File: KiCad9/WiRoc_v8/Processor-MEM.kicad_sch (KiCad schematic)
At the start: 28 parts

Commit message: etc
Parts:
- C46, C52: LCSC Part # (none) -> C15525; Manufacturer (none) -> Samsung Electro-Mechanics; ManufacturerPartNumber (none) -> CL05A106MQ5NUNC
- C47, C48, C53, C54, C58, C59: LCSC Part # (none) -> C52923; Manufacturer (none) -> Samsung Electro-Mechanics; ManufacturerPartNumber (none) -> CL05A105KA5NQNC
- U11: value ~ -> AllwinnerH3
- U12: value ~ -> DDR3
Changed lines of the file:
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@@
 			)
 		)
-		(property "Datasheet" "~"
+		(property "Datasheet" "https://jlcpcb.com/api/file/downloadByFileSystemAccessId/8579707174974914560"
 			(at 218.44 43.18 0)
 			(effects
@@
 		)
 		(property "Description" ""
+			(at 218.44 43.18 0)
+			(effects
+				(font
+					(size 1.27 1.27)
+				)
+				(hide yes)
+			)
+		)
+		(property "LCSC Part #" "C52923"
+			(at 218.44 43.18 0)
+			(effects
+				(font
+					(size 1.27 1.27)
+				)
+				(hide yes)
+			)
+		)
+		(property "Manufacturer" "Samsung Electro-Mechanics"
+			(at 218.44 43.18 0)
+			(effects
+				(font
+					(size 1.27 1.27)
+				)
+				(hide yes)
+			)
+		)
+		(property "ManufacturerPartNumber" "CL05A105KA5NQNC"
 			(at 218.44 43.18 0)
 			(effects
@@
 			)
 		)
-		(property "Datasheet" "~"
+		(property "Datasheet" "https://jlcpcb.com/api/file/downloadByFileSystemAccessId/8579707174974914560"
 			(at 207.01 91.44 0)
 			(effects
@@
 		)
 		(property "Description" ""
+			(at 207.01 91.44 0)
+			(effects
+				(font
+					(size 1.27 1.27)
+				)
+				(hide yes)
+			)
+		)
+		(property "LCSC Part #" "C52923"
+			(at 207.01 91.44 0)
+			(effects
+				(font
+					(size 1.27 1.27)
+				)
+				(hide yes)
+			)
+		)
+		(property "Manufacturer" "Samsung Electro-Mechanics"
+			(at 207.01 91.44 0)
+			(effects
+				(font
+					(size 1.27 1.27)
+				)
+				(hide yes)
+			)
+		)
+		(property "ManufacturerPartNumber" "CL05A105KA5NQNC"
 			(at 207.01 91.44 0)
 			(effects
@@
 			)
 		)
-		(property "Datasheet" "~"
+		(property "Datasheet" "https://jlcpcb.com/api/file/downloadByFileSystemAccessId/8579707174974914560"
 			(at 229.87 43.18 0)
 			(effects
@@
 		)
 		(property "Description" ""
+			(at 229.87 43.18 0)
+			(effects
+				(font
+					(size 1.27 1.27)
+				)
+				(hide yes)
+			)
+		)
+		(property "LCSC Part #" "C52923"
+			(at 229.87 43.18 0)
+			(effects
+				(font
+					(size 1.27 1.27)
+				)
+				(hide yes)
+			)
+		)
+		(property "Manufacturer" "Samsung Electro-Mechanics"
+			(at 229.87 43.18 0)
+			(effects
+				(font
+					(size 1.27 1.27)
+				)
+				(hide yes)
+			)
+		)
+		(property "ManufacturerPartNumber" "CL05A105KA5NQNC"
 			(at 229.87 43.18 0)
 			(effects
@@
 			)
 		)
+		(property "LCSC Part #" "C15525"
+			(at 207.01 67.31 0)
+			(effects
+				(font
+					(size 1.27 1.27)
+				)
+				(hide yes)
+			)
+		)
+		(property "Manufacturer" "Samsung Electro-Mechanics"
+			(at 207.01 67.31 0)
+			(effects
+				(font
+					(size 1.27 1.27)
+				)
+				(hide yes)
+			)
+		)
+		(property "ManufacturerPartNumber" "CL05A106MQ5NUNC"
+			(at 207.01 67.31 0)
+			(effects
+				(font
+					(size 1.27 1.27)
+				)
+				(hide yes)
+			)
+		)
 		(pin "2"
 		)
@@
 			)
 		)
-		(property "Datasheet" "~"
+		(property "Datasheet" "https://jlcpcb.com/api/file/downloadByFileSystemAccessId/8579707174974914560"
 			(at 229.87 67.31 0)
 			(effects
@@
 		)
 		(property "Description" ""
+			(at 229.87 67.31 0)
+			(effects
+				(font
+					(size 1.27 1.27)
+				)
+				(hide yes)
+			)
+		)
+		(property "LCSC Part #" "C52923"
+			(at 229.87 67.31 0)
+			(effects
+				(font
+					(size 1.27 1.27)
+				)
+				(hide yes)
+			)
+		)
+		(property "Manufacturer" "Samsung Electro-Mechanics"
+			(at 229.87 67.31 0)
+			(effects
+				(font
+					(size 1.27 1.27)
+				)
+				(hide yes)
+			)
+		)
+		(property "ManufacturerPartNumber" "CL05A105KA5NQNC"
 			(at 229.87 67.31 0)
 			(effects
@@
 			)
 		)
+		(property "LCSC Part #" "C15525"
+			(at 207.01 43.18 0)
+			(effects
+				(font
+					(size 1.27 1.27)
+				)
+				(hide yes)
+			)
+		)
+		(property "Manufacturer" "Samsung Electro-Mechanics"
+			(at 207.01 43.18 0)
+			(effects
+				(font
+					(size 1.27 1.27)
+				)
+				(hide yes)
+			)
+		)
+		(property "ManufacturerPartNumber" "CL05A106MQ5NUNC"
+			(at 207.01 43.18 0)
+			(effects
+				(font
+					(size 1.27 1.27)
+				)
+				(hide yes)
+			)
+		)
 		(pin "2"
 		)
@@
 			)
 		)
-		(property "Datasheet" "~"
+		(property "Datasheet" "https://jlcpcb.com/api/file/downloadByFileSystemAccessId/8579707174974914560"
 			(at 218.44 91.44 0)
 			(effects
@@
 		)
 		(property "Description" ""
+			(at 218.44 91.44 0)
+			(effects
+				(font
+					(size 1.27 1.27)
+				)
+				(hide yes)
+			)
+		)
+		(property "LCSC Part #" "C52923"
+			(at 218.44 91.44 0)
+			(effects
+				(font
+					(size 1.27 1.27)
+				)
+				(hide yes)
+			)
+		)
+		(property "Manufacturer" "Samsung Electro-Mechanics"
+			(at 218.44 91.44 0)
+			(effects
+				(font
+					(size 1.27 1.27)
+				)
+				(hide yes)
+			)
+		)
+		(property "ManufacturerPartNumber" "CL05A105KA5NQNC"
 			(at 218.44 91.44 0)
 			(effects
@@
 			)
 		)
-		(property "Datasheet" "~"
+		(property "Datasheet" "https://jlcpcb.com/api/file/downloadByFileSystemAccessId/8579707174974914560"
 			(at 218.44 67.31 0)
 			(effects
@@
 		)
 		(property "Description" ""
+			(at 218.44 67.31 0)
+			(effects
+				(font
+					(size 1.27 1.27)
+				)
+				(hide yes)
+			)
+		)
+		(property "LCSC Part #" "C52923"
+			(at 218.44 67.31 0)
+			(effects
+				(font
+					(size 1.27 1.27)
+				)
+				(hide yes)
+			)
+		)
+		(property "Manufacturer" "Samsung Electro-Mechanics"
+			(at 218.44 67.31 0)
+			(effects
+				(font
+					(size 1.27 1.27)
+				)
+				(hide yes)
+			)
+		)
+		(property "ManufacturerPartNumber" "CL05A105KA5NQNC"
 			(at 218.44 67.31 0)
 			(effects
@@
 			)
 		)
-		(property "Value" "~"
+		(property "Value" "DDR3"
 			(at 102.87 25.4 0)
 			(effects
@@
 			)
 		)
-		(property "Value" "~"
+		(property "Value" "AllwinnerH3"
 			(at 45.72 64.77 0)
 			(effects

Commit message: add bom
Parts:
- C28, C29, C49, C50, C51, C55, C56, C57, C60, C61, C62, C63: IncludeInBOM (none) -> TRUE; JLCBasicExtended (none) -> Basic; LCSC Part # (none) -> C1525; Manufacturer (none) -> Samsung Electro-Mechanics; ManufacturerPartNumber (none) -> CL05B104KO5NNNC; Package (none) -> 0402
- C46, C47, C48, C52, C53, C54, C58, C59: IncludeInBOM (none) -> TRUE; JLCBasicExtended (none) -> Basic; Package (none) -> 0402
- R18, R20, R21: IncludeInBOM (none) -> TRUE; JLCBasicExtended (none) -> Extended; LCSC Part # (none) -> C25094; Manufacturer (none) -> Uniroyal Elec; ManufacturerPartNumber (none) -> 0402WGF2400TCE; Package (none) -> 0402
- R36, R37: IncludeInBOM (none) -> TRUE; JLCBasicExtended (none) -> Basic; LCSC Part # (none) -> C4109; Manufacturer (none) -> Uniroyal Elec; ManufacturerPartNumber (none) -> 0402WGF2001TCE; Package (none) -> 0402
- R38: IncludeInBOM (none) -> TRUE; JLCBasicExtended (none) -> Basic; LCSC Part # (none) -> C25076; Manufacturer (none) -> Uniroyal Elec; ManufacturerPartNumber (none) -> 0402WGF1000TCE; Package (none) -> 0402
- U11: IncludeInBOM (none) -> TRUE; JLCBasicExtended (none) -> Extended; LCSC Part # (none) -> C94644; Manufacturer (none) -> Allwinner; ManufacturerPartNumber (none) -> H3; Package (none) -> FBGA-347(14x14)
- U12: IncludeInBOM (none) -> TRUE; JLCBasicExtended (none) -> Extended; LCSC Part # (none) -> C2841151; Manufacturer (none) -> Micron Tech; ManufacturerPartNumber (none) -> MT41K128M16JT-107:K; Note (none) -> C2909894 H5TQ2G63GFR-TEC 96ball FBGA compatible pinout : 0 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; Package (none) -> FBGA-96(8x14)

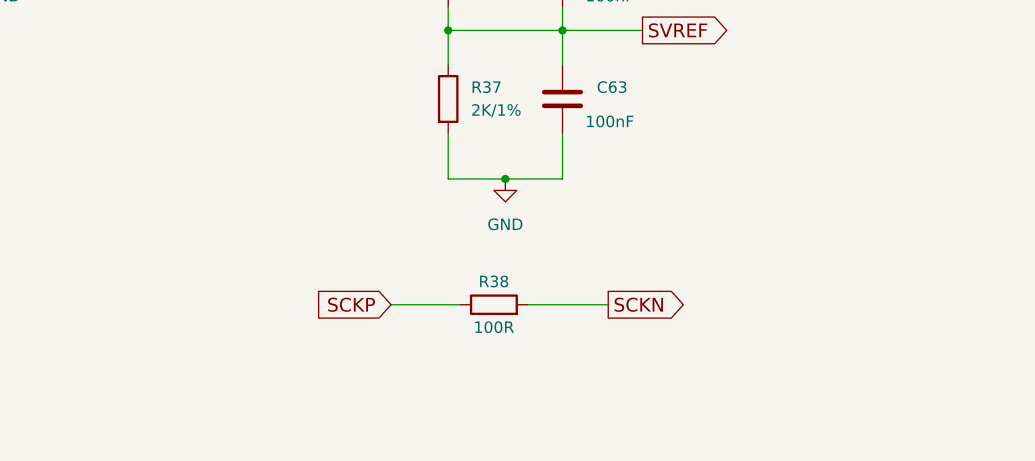
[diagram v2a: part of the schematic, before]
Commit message: change tracewidth for mem, add nettie for better length calculation
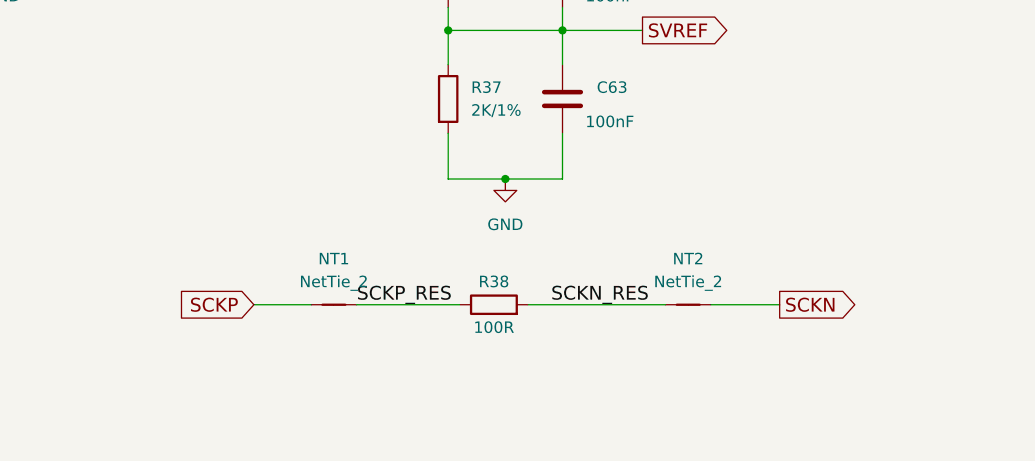
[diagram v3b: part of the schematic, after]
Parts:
- added NT1, NT2: NetTie_2, WiRoc:NetTie-2_SMD_Pad0.12mm, symbol Device:NetTie_2
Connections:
- net SCKN: now also NT2.2; no longer R38.2
- net SCKP: now also NT1.1; no longer R38.1
- new net SCKN_RES: NT2.1, R38.2
- new net SCKP_RES: NT1.2, R38.1
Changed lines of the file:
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@@
 	(wire
 		(pts
-			(xy 198.12 161.29) (xy 205.74 161.29)
+			(xy 182.88 161.29) (xy 189.23 161.29)
 		)
 		(stroke
@@
 	(wire
 		(pts
+			(xy 233.68 161.29) (xy 241.3 161.29)
+		)
+		(stroke
+			(width 0)
+			(type default)
+		)
+	)
+	(wire
+		(pts
 			(xy 229.87 95.25) (xy 241.3 95.25)
 		)
@@
 	(wire
 		(pts
-			(xy 213.36 161.29) (xy 222.25 161.29)
+			(xy 213.36 161.29) (xy 228.6 161.29)
 		)
 		(stroke
@@
 	(wire
 		(pts
+			(xy 194.31 161.29) (xy 205.74 161.29)
+		)
+		(stroke
+			(width 0)
+			(type default)
+		)
+	)
+	(wire
+		(pts
 			(xy 133.35 115.57) (xy 133.35 118.11)
 		)
@@
 		)
 	)
+	(label "SCKN_RES"
+		(at 215.9 161.29 0)
+		(effects
+			(font
+				(size 1.524 1.524)
+			)
+			(justify left bottom)
+		)
+	)
 	(label "SA7"
 		(at 74.93 46.99 0)
@@
 		)
 	)
+	(label "SCKP_RES"
+		(at 194.31 161.29 0)
+		(effects
+			(font
+				(size 1.524 1.524)
+			)
+			(justify left bottom)
+		)
+	)
 	(label "SA4"
 		(at 74.93 39.37 0)
@@
 	(global_label "SCKN"
 		(shape output)
-		(at 222.25 161.29 0)
+		(at 241.3 161.29 0)
 		(fields_autoplaced yes)
 		(effects
@@
 		)
 		(property "Intersheetrefs" "${INTERSHEET_REFS}"
-			(at 231.1428 161.29 0)
+			(at 250.1928 161.29 0)
 			(effects
 				(font
@@
 	(global_label "SCKP"
 		(shape input)
-		(at 198.12 161.29 180)
+		(at 182.88 161.29 180)
 		(fields_autoplaced yes)
 		(effects
@@
 		)
 		(property "Intersheetrefs" "${INTERSHEET_REFS}"
-			(at 189.2998 161.29 0)
+			(at 174.0598 161.29 0)
 			(effects
 				(font
@@
 	)
 	(symbol
+		(lib_id "Device:NetTie_2")
+		(at 191.77 161.29 0)
+		(unit 1)
+		(exclude_from_sim no)
+		(in_bom no)
+		(on_board yes)
+		(dnp no)
+		(fields_autoplaced yes)
+		(property "Reference" "NT1"
+			(at 191.77 156.21 0)
+			(effects
+				(font
+					(size 1.27 1.27)
+				)
+			)
+		)
+		(property "Value" "NetTie_2"
+			(at 191.77 158.75 0)
+			(effects
+				(font
+					(size 1.27 1.27)
+				)
+			)
+		)
+		(property "Footprint" "WiRoc:NetTie-2_SMD_Pad0.12mm"
+			(at 191.77 161.29 0)
+			(effects
+				(font
+					(size 1.27 1.27)
+				)
+				(hide yes)
+			)
+		)
+		(property "Datasheet" "~"
+			(at 191.77 161.29 0)
+			(effects
+				(font
+					(size 1.27 1.27)
+				)
+				(hide yes)
+			)
+		)
+		(property "Description" "Net tie, 2 pins"
+			(at 191.77 161.29 0)
+			(effects
+				(font
+					(size 1.27 1.27)
+				)
+				(hide yes)
+			)
+		)
+		(pin "2"
+		)
+		(pin "1"
+		)
+		(instances
+			(project ""
+				(path "/8ba0b499-eaca-4cd5-a002-c6bdb610cc8c/3131bab2-0774-414a-a557-ba7c663eebf6"
+					(reference "NT1")
+					(unit 1)
+				)
+			)
+		)
+	)
+	(symbol
 		(lib_id "Device:C")
 		(at 92.71 102.87 0)
@@
 					(unit 1)
 				)
+			)
+		)
+	)
+	(symbol
+		(lib_id "Device:NetTie_2")
+		(at 231.14 161.29 0)
+		(unit 1)
+		(exclude_from_sim no)
+		(in_bom no)
+		(on_board yes)
+		(dnp no)
+		(fields_autoplaced yes)
+		(property "Reference" "NT2"
+			(at 231.14 156.21 0)
+			(effects
+				(font
+					(size 1.27 1.27)
+				)
+			)
+		)
+		(property "Value" "NetTie_2"
+			(at 231.14 158.75 0)
+			(effects
+				(font
+					(size 1.27 1.27)
+				)
+			)
+		)
+		(property "Footprint" "WiRoc:NetTie-2_SMD_Pad0.12mm"
+			(at 231.14 161.29 0)
+			(effects
+				(font
+					(size 1.27 1.27)
+				)
+				(hide yes)
+			)
+		)
+		(property "Datasheet" "~"
+			(at 231.14 161.29 0)
+			(effects
+				(font
+					(size 1.27 1.27)
+				)
+				(hide yes)
+			)
+		)
+		(property "Description" "Net tie, 2 pins"
+			(at 231.14 161.29 0)
+			(effects
+				(font
+					(size 1.27 1.27)
+				)
+				(hide yes)
+			)
+		)
+		(pin "1"
+		)
+		(pin "2"
+		)
+		(instances
+			(project ""
+				(path "/8ba0b499-eaca-4cd5-a002-c6bdb610cc8c/3131bab2-0774-414a-a557-ba7c663eebf6"
+					(reference "NT2")
+					(unit 1)
+				)

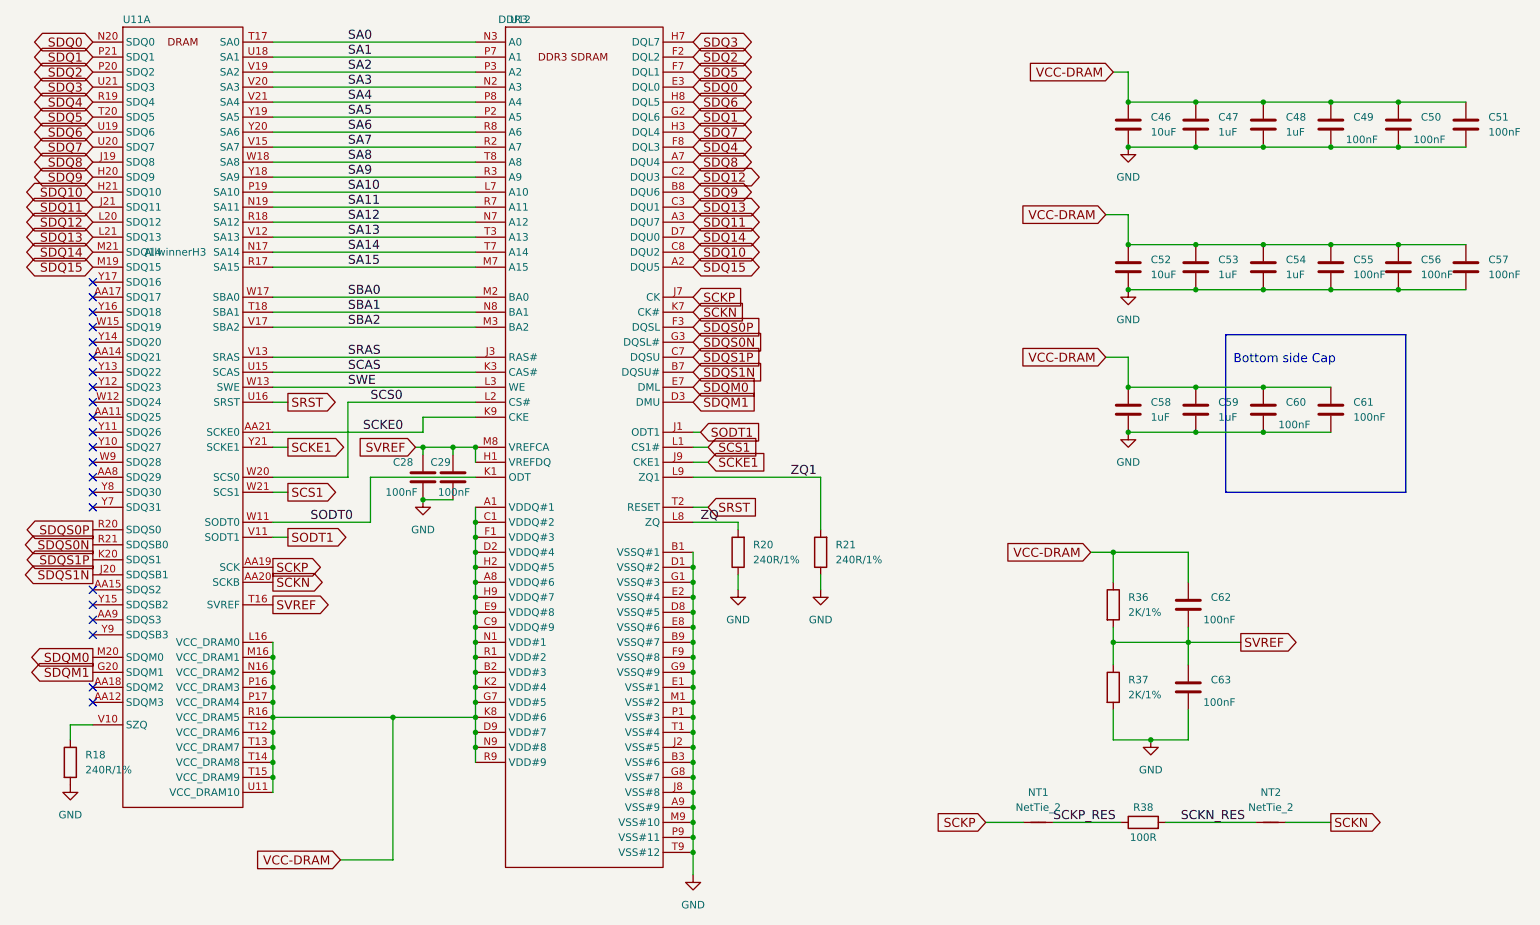
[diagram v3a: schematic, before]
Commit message: add esp32hosted-c5 board
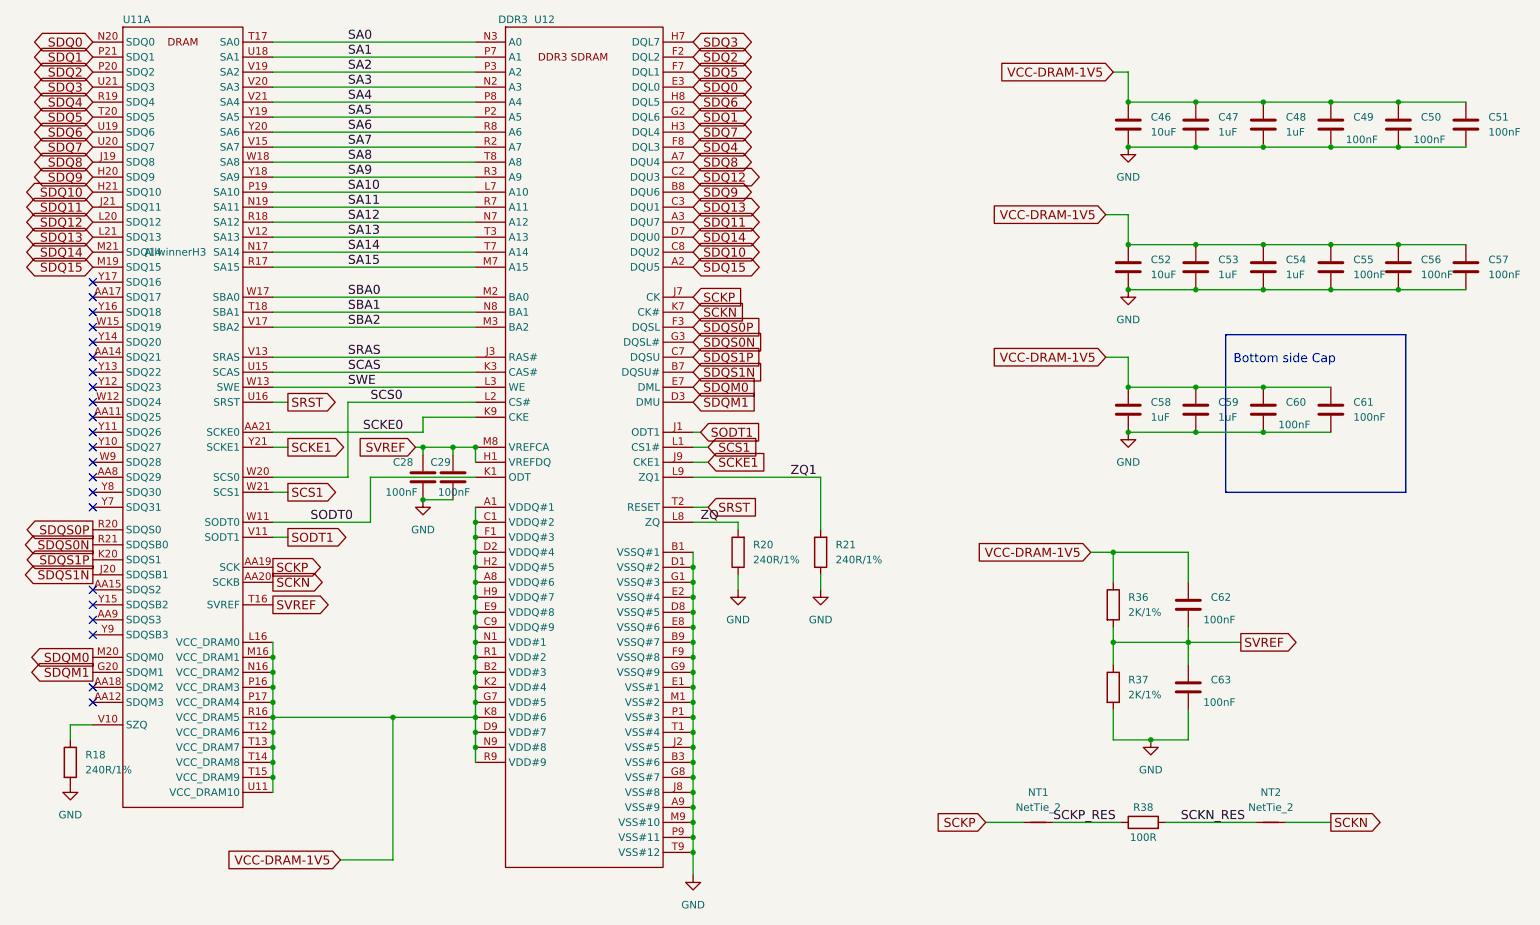
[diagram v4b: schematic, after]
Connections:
- net VCC-DRAM renamed VCC-DRAM-1V5
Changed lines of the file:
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@@
 		)
 	)
-	(global_label "VCC-DRAM"
+	(global_label "VCC-DRAM-1V5"
 		(shape input)
 		(at 203.2 58.42 180)
@@
 		)
 		(property "Intersheetrefs" "${INTERSHEET_REFS}"
-			(at 188.066 58.42 0)
+			(at 181.97 58.42 0)
 			(effects
 				(font
@@
 		)
 	)
-	(global_label "VCC-DRAM"
+	(global_label "VCC-DRAM-1V5"
 		(shape input)
 		(at 73.66 167.64 180)
@@
 		)
 		(property "Intersheetrefs" "${INTERSHEET_REFS}"
-			(at 58.526 167.64 0)
+			(at 52.43 167.64 0)
 			(effects
 				(font
@@
 		)
 	)
-	(global_label "VCC-DRAM"
+	(global_label "VCC-DRAM-1V5"
 		(shape input)
 		(at 203.2 82.55 180)
@@
 		)
 		(property "Intersheetrefs" "${INTERSHEET_REFS}"
-			(at 188.066 82.55 0)
+			(at 181.97 82.55 0)
 			(effects
 				(font
@@
 		)
 	)
-	(global_label "VCC-DRAM"
+	(global_label "VCC-DRAM-1V5"
 		(shape input)
 		(at 204.47 34.29 180)
@@
 		)
 		(property "Intersheetrefs" "${INTERSHEET_REFS}"
-			(at 189.336 34.29 0)
+			(at 183.24 34.29 0)
 			(effects
 				(font
@@
 		)
 	)
-	(global_label "VCC-DRAM"
+	(global_label "VCC-DRAM-1V5"
 		(shape input)
 		(at 200.66 115.57 180)
@@
 		)
 		(property "Intersheetrefs" "${INTERSHEET_REFS}"
-			(at 185.526 115.57 0)
+			(at 179.43 115.57 0)
 			(effects
 				(font
@@
 		(dnp no)
 		(property "Reference" "U12"
-			(at 104.14 25.4 0)
+			(at 108.204 25.4 0)
 			(effects
 				(font
